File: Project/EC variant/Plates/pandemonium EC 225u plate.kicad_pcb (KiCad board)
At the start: 2 copper layers, 199.9 x 81 mm, 37 parts

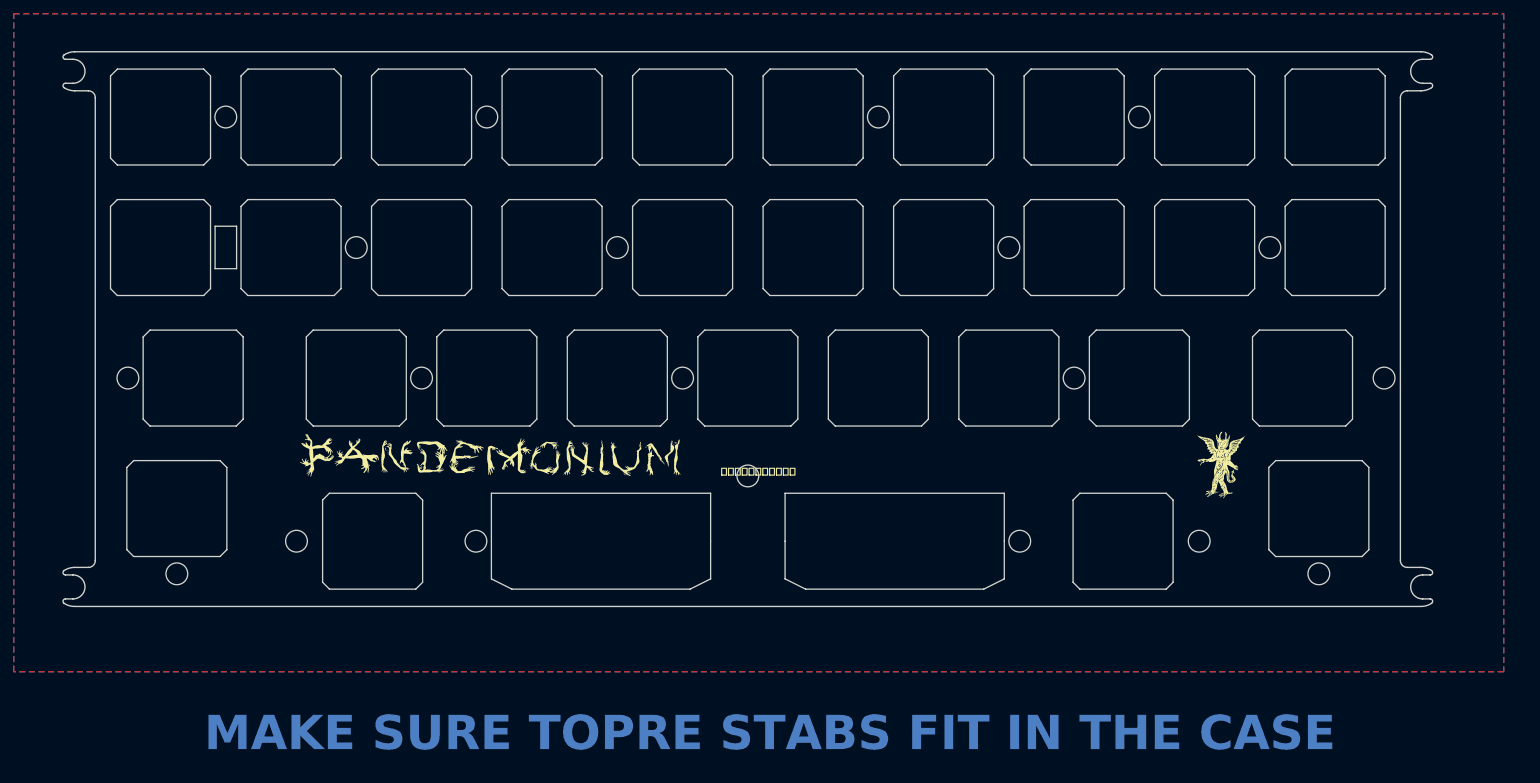
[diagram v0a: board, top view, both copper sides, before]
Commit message: changes to topre version and BLE version
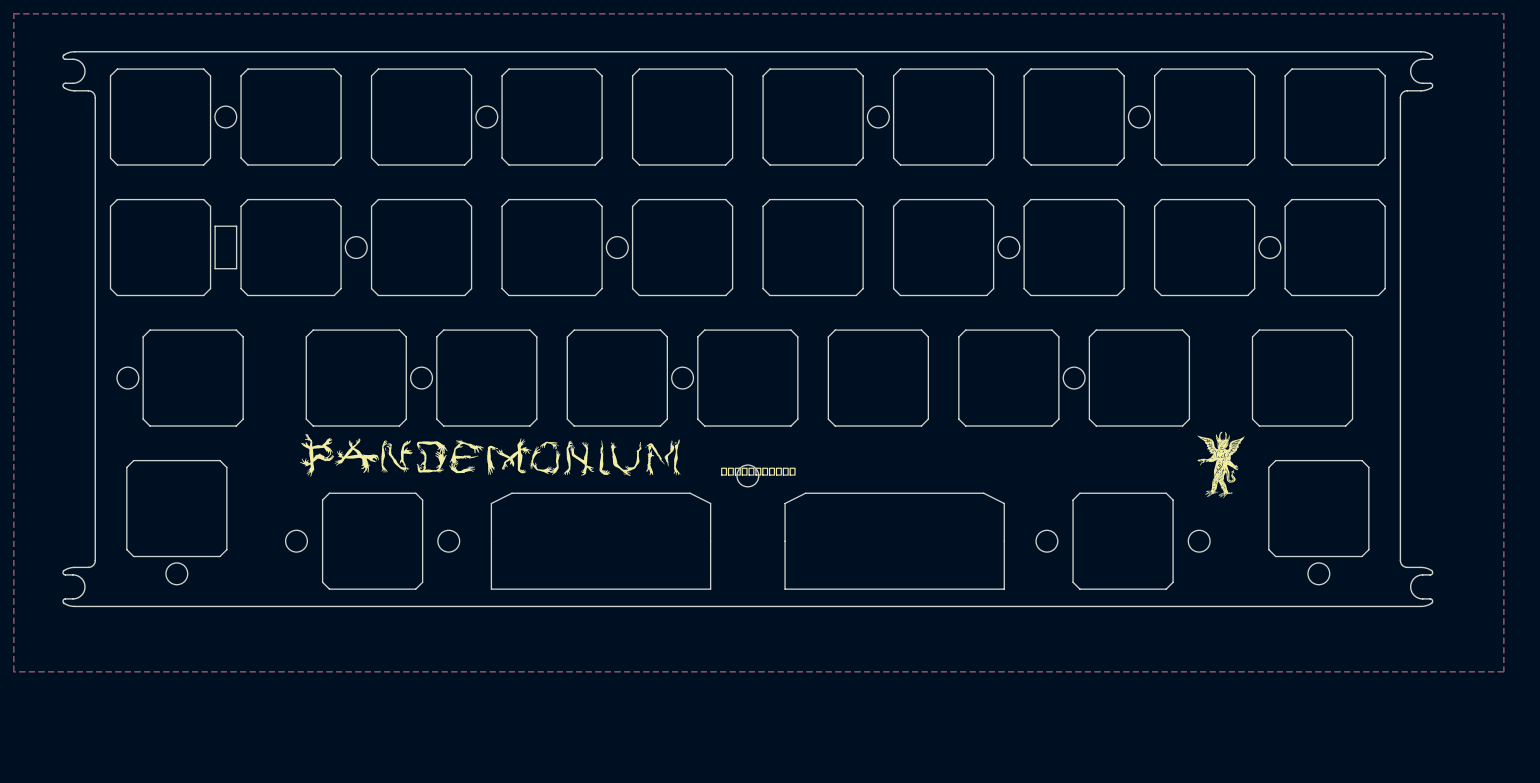
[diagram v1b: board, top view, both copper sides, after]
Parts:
- turned REF** to 180 degrees (x2)
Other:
- outline, holes or cut-outs redrawn
- board text removed: "MAKE SURE TOPRE STABS FIT IN THE CASE"
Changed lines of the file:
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@@
   )
   (footprint "cipulot_parts:ecs_plate_cut_2U" (layer "F.Cu")
-    (at 148.43125 95.25)
+    (at 148.43125 95.25 180)
     (descr " StepUp generated footprint")
     (attr smd)
@@
   )
   (footprint "cipulot_parts:ecs_plate_cut_2U" (layer "F.Cu")
-    (at 105.56875 95.25)
+    (at 105.56875 95.25 180)
     (descr " StepUp generated footprint")
     (attr smd)
@@
     )
   )
-  (gr_circle (center 219.86875 71.4375) (end 219.86875 69.85)
-    (stroke (width 0.1) (type default)) (fill none) (layer "Edge.Cuts"))
   (gr_circle (center 61.11875 95.25) (end 61.11875 93.6625)
     (stroke (width 0.1) (type default)) (fill none) (layer "Edge.Cuts"))
@@
   (gr_circle (center 107.95 52.3875) (end 107.95 50.8)
     (stroke (width 0.1) (type default)) (fill none) (layer "Edge.Cuts"))
-  (gr_circle (center 87.3125 95.25) (end 87.3125 93.6625)
+  (gr_circle (center 83.34375 95.25) (end 83.34375 93.6625)
     (stroke (width 0.1) (type default)) (fill none) (layer "Edge.Cuts"))
   (gr_arc (start 31.75 98.075) (mid 31.457107 98.782107) (end 30.75 99.075)
@@
   (gr_line (start 225.499442 24.9125) (end 226.606464 24.9125)
     (stroke (width 0.2) (type solid)) (layer "Edge.Cuts"))
-  (gr_circle (center 166.6875 95.25) (end 166.6875 93.6625)
+  (gr_circle (center 170.65625 95.25) (end 170.65625 93.6625)
     (stroke (width 0.1) (type default)) (fill none) (layer "Edge.Cuts"))
   (gr_line (start 27.393534 100.175) (end 28.500555 100.175)
@@
   (gr_line (start 223.25 29.5125) (end 225.249998 29.5125)
     (stroke (width 0.2) (type solid)) (layer "Edge.Cuts"))
-  (gr_text "MAKE SURE TOPRE STABS FIT IN THE CASE" (at 47.625 126.20625) (layer "B.Cu")
-    (effects (font (size 5 5) (thickness 0.3) bold) (justify left bottom))
-  )
   (gr_text "JLCJLCJLCJLC" (at 127 25.4) (layer "B.SilkS")
     (effects (font (size 1 1) (thickness 0.15)))
